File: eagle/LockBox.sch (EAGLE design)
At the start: 7 parts

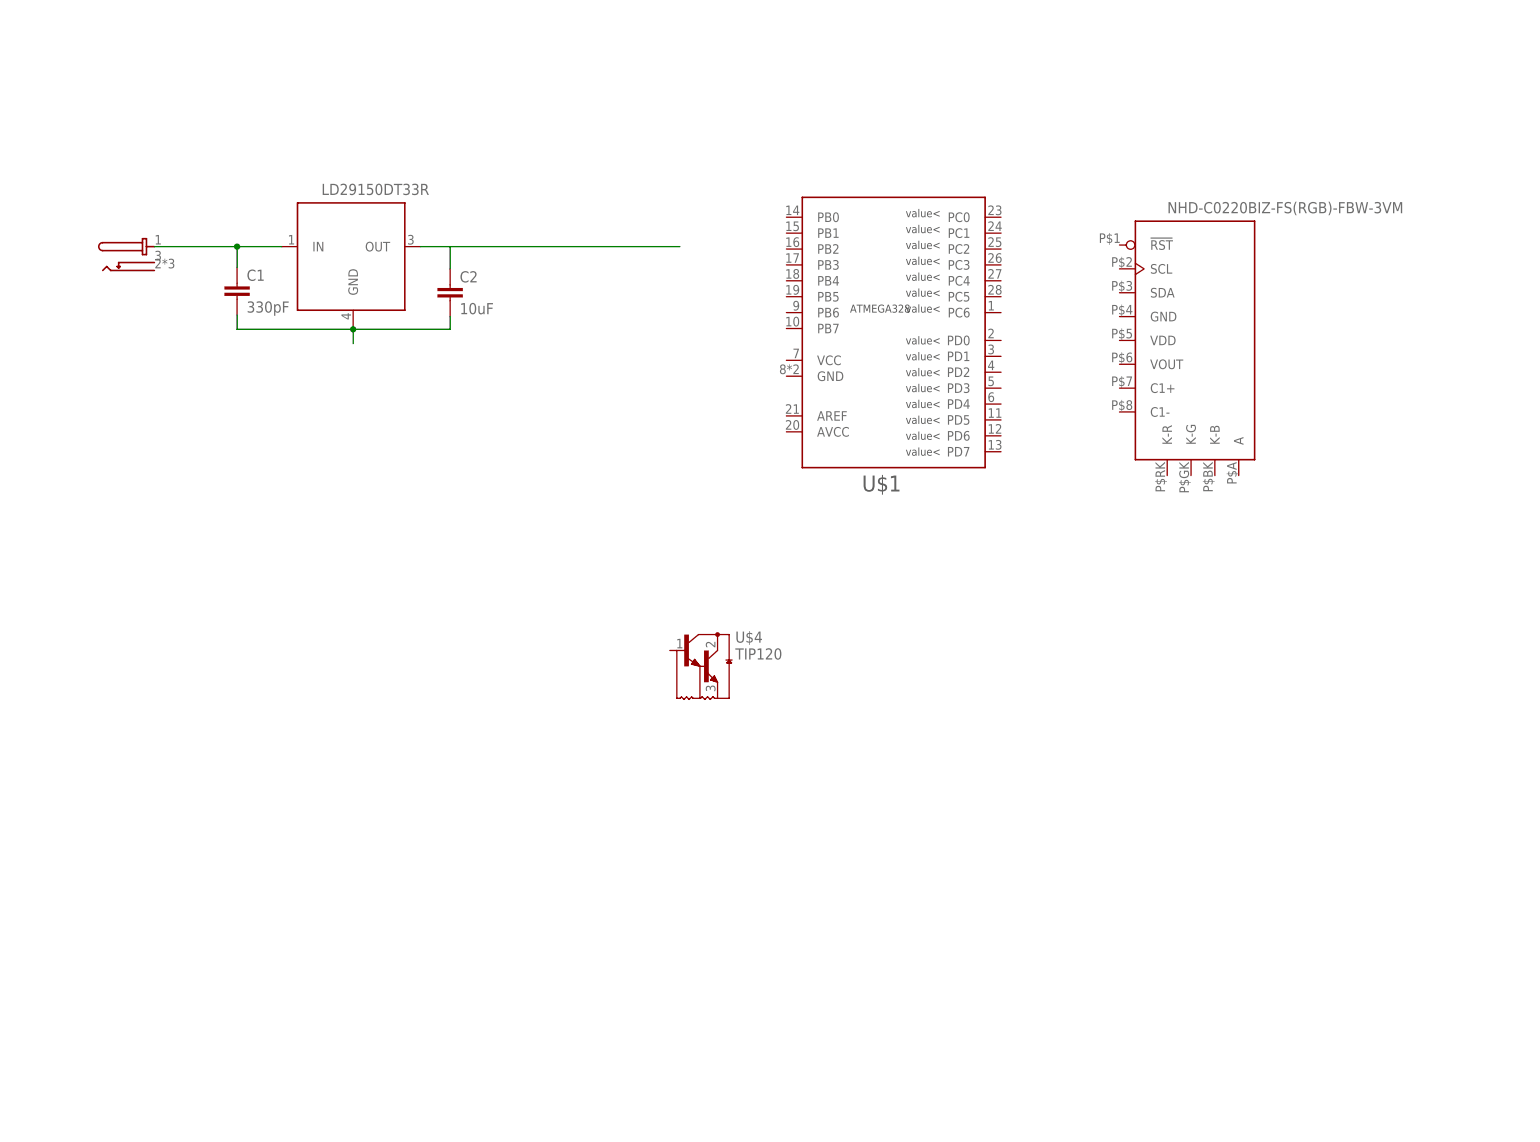
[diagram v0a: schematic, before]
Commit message: Finished the powersupply and LDO portion of the LockBox.sch, Added pwr/gnd and bypass cap to the ATMEL chip, updateded I2C pin attributes and added I2C bus.
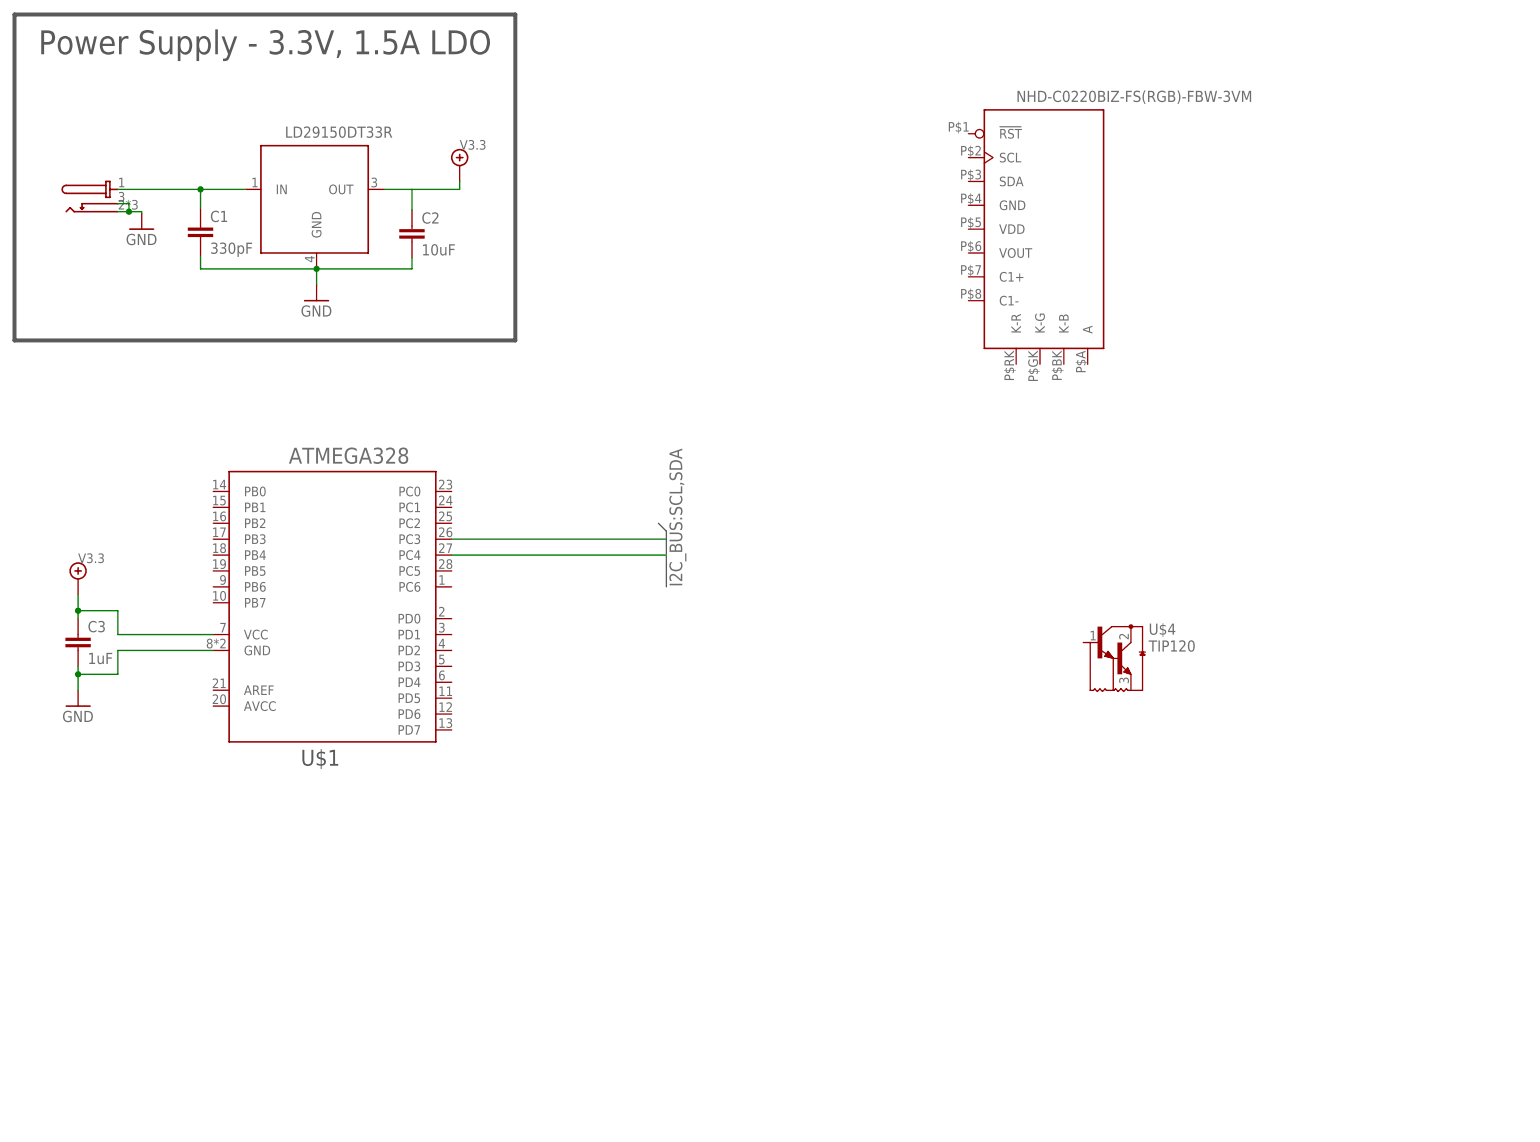
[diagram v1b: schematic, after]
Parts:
- added C3: 1uF, LockBox:C
- U$1: PC3 (none) -> SCL; PC4 (none) -> SDA
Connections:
- removed net N$2: C2.1, U$2.OUT
- removed net N$3: C1.2, C2.2, U$2.GND
- new net GND: C1.2, C2.2, C3.2, U$1.GND, U$2.GND, U$3.GND@1, U$3.GND@2
- new net P$1: C2.1, C3.1, U$1.VCC, U$2.OUT
- new net SCL: U$1.PC3
- new net SDA: U$1.PC4
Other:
- note added: "Power Supply - 3.3V, 1.5A LDO"
- moved on the sheet: C1, C2, U$4
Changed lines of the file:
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@@
 <setting verticaltext="up"/>
 </settings>
-<grid distance="0.005" unitdist="inch" unit="inch" style="lines" multiple="1" display="yes" altdistance="0.01" altunitdist="inch" altunit="inch"/>
+<grid distance="0.05" unitdist="inch" unit="inch" style="lines" multiple="1" display="yes" altdistance="0.01" altunitdist="inch" altunit="inch"/>
 <layers>
 <layer number="1" name="Top" color="4" fill="1" visible="no" active="no"/>
@@
 <parts>
 <part name="FRAME1" library="LockBox" deviceset="FRAME-LETTER" device=""/>
-<part name="U$1" library="LockBox" deviceset="ATMEGA328" device=""/>
 <part name="U$2" library="LockBox" deviceset="LD29150" device="" technology="DT33R"/>
 <part name="U$3" library="LockBox" deviceset="PJ_075" device="" technology="DH"/>
@@
 <part name="C1" library="LockBox" deviceset="C" device="" value="330pF"/>
 <part name="C2" library="LockBox" deviceset="C" device="" value="10uF"/>
+<part name="GND1" library="LockBox" deviceset="GND" device=""/>
+<part name="GND2" library="LockBox" deviceset="GND" device=""/>
+<part name="V1" library="LockBox" deviceset="V3.3" device=""/>
+<part name="U$1" library="LockBox" deviceset="ATMEGA328" device="">
+<attribute name="PC3" value="SCL"/>
+<attribute name="PC4" value="SDA"/>
+</part>
+<part name="C3" library="LockBox" deviceset="C" device="" value="1uF"/>
+<part name="GND3" library="LockBox" deviceset="GND" device=""/>
+<part name="V2" library="LockBox" deviceset="V3.3" device=""/>
 </parts>
 <sheets>
 <sheet>
 <plain>
+<wire x1="91.44" y1="180.34" x2="91.44" y2="128.27" width="0.635" layer="97"/>
+<wire x1="91.44" y1="128.27" x2="11.43" y2="128.27" width="0.635" layer="97"/>
+<wire x1="11.43" y1="128.27" x2="11.43" y2="180.34" width="0.635" layer="97"/>
+<wire x1="11.43" y1="180.34" x2="91.44" y2="180.34" width="0.635" layer="97"/>
+<text x="15.24" y="173.99" size="3.81" layer="97">Power Supply - 3.3V, 1.5A LDO</text>
 </plain>
 <instances>
 <instance part="FRAME1" gate="G$1" x="0" y="0"/>
 <instance part="FRAME1" gate="G$2" x="147.32" y="0"/>
-<instance part="U$1" gate="G$1" x="151.892" y="132.08"/>
-<instance part="U$2" gate="G$1" x="61.722" y="141.986"/>
-<instance part="U$3" gate="G$1" x="31.877" y="142.621"/>
-<instance part="U$4" gate="G$1" x="121.92" y="76.2"/>
-<instance part="U$5" gate="G$1" x="200.66" y="129.54"/>
-<instance part="C1" gate="G$1" x="46.99" y="137.414"/>
-<instance part="C2" gate="G$1" x="81.026" y="137.16"/>
+<instance part="U$2" gate="G$1" x="55.88" y="151.13"/>
+<instance part="U$3" gate="G$1" x="26.035" y="151.765"/>
+<instance part="U$4" gate="G$1" x="187.96" y="77.47"/>
+<instance part="U$5" gate="G$1" x="176.53" y="147.32"/>
+<instance part="C1" gate="G$1" x="41.148" y="146.812"/>
+<instance part="C2" gate="G$1" x="74.93" y="146.558"/>
+<instance part="GND1" gate="1" x="59.69" y="134.62"/>
+<instance part="GND2" gate="1" x="31.75" y="146.05"/>
+<instance part="V1" gate="G1" x="82.55" y="156.21"/>
+<instance part="U$1" gate="G$1" x="62.23" y="88.265">
+<attribute name="PC3" x="62.23" y="88.265" size="1.778" layer="96" display="off"/>
+<attribute name="PC4" x="62.23" y="88.265" size="1.778" layer="96" display="off"/>
+</instance>
+<instance part="C3" gate="G$1" x="21.59" y="81.28"/>
+<instance part="GND3" gate="1" x="21.59" y="69.85"/>
+<instance part="V2" gate="G1" x="21.59" y="90.17"/>
 </instances>
 <busses>
+<bus name="I2C_BUS:SCL,SDA">
+<segment>
+<wire x1="114.3" y1="99.06" x2="115.57" y2="97.79" width="0.762" layer="92"/>
+<wire x1="115.57" y1="97.79" x2="115.57" y2="88.9" width="0.762" layer="92"/>
+<label x="118.11" y="88.9" size="2.032" layer="95" rot="R90"/>
+</segment>
+</bus>
 </busses>
 <nets>
@@
 <segment>
 <pinref part="C1" gate="G$1" pin="1"/>
-<wire x1="46.99" y1="139.954" x2="46.99" y2="143.256" width="0.1524" layer="91"/>
+<wire x1="41.148" y1="149.352" x2="41.148" y2="152.4" width="0.1524" layer="91"/>
 <pinref part="U$2" gate="G$1" pin="IN"/>
-<wire x1="46.99" y1="143.256" x2="54.102" y2="143.256" width="0.1524" layer="91"/>
-<wire x1="46.99" y1="143.256" x2="33.782" y2="143.256" width="0.1524" layer="91"/>
-<junction x="46.99" y="143.256"/>
+<wire x1="41.148" y1="152.4" x2="48.26" y2="152.4" width="0.1524" layer="91"/>
+<wire x1="41.148" y1="152.4" x2="27.94" y2="152.4" width="0.1524" layer="91"/>
+<junction x="41.148" y="152.4"/>
 <pinref part="U$3" gate="G$1" pin="PWR"/>
 </segment>
 </net>
-<net name="N$2" class="0">
+<net name="GND" class="0">
+<segment>
+<pinref part="C2" gate="G$1" pin="2"/>
+<wire x1="74.93" y1="141.478" x2="74.93" y2="139.7" width="0.1524" layer="91"/>
+<pinref part="U$2" gate="G$1" pin="GND"/>
+<wire x1="74.93" y1="139.7" x2="59.69" y2="139.7" width="0.1524" layer="91"/>
+<pinref part="C1" gate="G$1" pin="2"/>
+<wire x1="59.69" y1="139.7" x2="41.148" y2="139.7" width="0.1524" layer="91"/>
+<wire x1="41.148" y1="139.7" x2="41.148" y2="141.732" width="0.1524" layer="91"/>
+<junction x="59.69" y="139.7"/>
+<wire x1="59.69" y1="139.7" x2="59.69" y2="137.16" width="0.1524" layer="91"/>
+<pinref part="GND1" gate="1" pin="GND"/>
+</segment>
+<segment>
+<pinref part="U$3" gate="G$1" pin="GND@1"/>
+<wire x1="27.94" y1="150.114" x2="29.718" y2="150.114" width="0.1524" layer="91"/>
+<wire x1="29.718" y1="150.114" x2="29.718" y2="148.844" width="0.1524" layer="91"/>
+<pinref part="U$3" gate="G$1" pin="GND@2"/>
+<wire x1="29.718" y1="148.844" x2="27.94" y2="148.844" width="0.1524" layer="91"/>
+<wire x1="29.718" y1="148.844" x2="31.75" y2="148.844" width="0.1524" layer="91"/>
+<wire x1="31.75" y1="148.844" x2="31.75" y2="148.59" width="0.1524" layer="91"/>
+<pinref part="GND2" gate="1" pin="GND"/>
+<junction x="29.718" y="148.844"/>
+</segment>
+<segment>
+<pinref part="U$1" gate="G$1" pin="GND"/>
+<wire x1="43.18" y1="78.74" x2="27.94" y2="78.74" width="0.1524" layer="91"/>
+<wire x1="27.94" y1="78.74" x2="27.94" y2="74.93" width="0.1524" layer="91"/>
+<wire x1="27.94" y1="74.93" x2="21.59" y2="74.93" width="0.1524" layer="91"/>
+<pinref part="C3" gate="G$1" pin="2"/>
+<wire x1="21.59" y1="74.93" x2="21.59" y2="76.2" width="0.1524" layer="91"/>
+<pinref part="GND3" gate="1" pin="GND"/>
+<wire x1="21.59" y1="74.93" x2="21.59" y2="72.39" width="0.1524" layer="91"/>
+<junction x="21.59" y="74.93"/>
+</segment>
+</net>
+<net name="P$1" class="0">
 <segment>
 <pinref part="C2" gate="G$1" pin="1"/>
-<wire x1="81.026" y1="139.7" x2="81.026" y2="143.256" width="0.1524" layer="91"/>
+<wire x1="74.93" y1="149.098" x2="74.93" y2="152.4" width="0.1524" layer="91"/>
 <pinref part="U$2" gate="G$1" pin="OUT"/>
-<wire x1="76.327" y1="143.256" x2="81.026" y2="143.256" width="0.1524" layer="91"/>
-<wire x1="81.026" y1="143.256" x2="117.729" y2="143.256" width="0.1524" layer="91"/>
-</segment>
-</net>
-<net name="N$3" class="0">
-<segment>
-<pinref part="C2" gate="G$1" pin="2"/>
-<wire x1="81.026" y1="132.08" x2="81.026" y2="130.048" width="0.1524" layer="91"/>
-<pinref part="U$2" gate="G$1" pin="GND"/>
-<wire x1="81.026" y1="130.048" x2="65.532" y2="130.048" width="0.1524" layer="91"/>
-<wire x1="65.532" y1="130.048" x2="65.532" y2="130.556" width="0.1524" layer="91"/>
-<pinref part="C1" gate="G$1" pin="2"/>
-<wire x1="65.532" y1="130.048" x2="46.99" y2="130.048" width="0.1524" layer="91"/>
-<wire x1="46.99" y1="130.048" x2="46.99" y2="132.334" width="0.1524" layer="91"/>
-<junction x="65.532" y="130.048"/>
-<wire x1="65.532" y1="130.048" x2="65.532" y2="127.762" width="0.1524" layer="91"/>
-</segment>
-</net>
+<wire x1="70.485" y1="152.4" x2="74.93" y2="152.4" width="0.1524" layer="91"/>
+<wire x1="74.93" y1="152.4" x2="82.55" y2="152.4" width="0.1524" layer="91"/>
+<pinref part="V1" gate="G1" pin="P$1"/>
+<wire x1="82.55" y1="152.4" x2="82.55" y2="153.67" width="0.1524" layer="91"/>
+</segment>
+<segment>
+<pinref part="U$1" gate="G$1" pin="VCC"/>
+<wire x1="43.18" y1="81.28" x2="27.94" y2="81.28" width="0.1524" layer="91"/>
+<wire x1="27.94" y1="81.28" x2="27.94" y2="85.09" width="0.1524" layer="91"/>
+<wire x1="27.94" y1="85.09" x2="21.59" y2="85.09" width="0.1524" layer="91"/>
+<pinref part="C3" gate="G$1" pin="1"/>
+<wire x1="21.59" y1="85.09" x2="21.59" y2="83.82" width="0.1524" layer="91"/>
+<pinref part="V2" gate="G1" pin="P$1"/>
+<wire x1="21.59" y1="85.09" x2="21.59" y2="87.63" width="0.1524" layer="91"/>
+<junction x="21.59" y="85.09"/>
+</segment>
+</net>
+<net name="SCL" class="0">
+<segment>
+<pinref part="U$1" gate="G$1" pin="PC3"/>
+<wire x1="115.57" y1="96.52" x2="81.28" y2="96.52" width="0.1524" layer="91"/>
+</segment>
+</net>
+<net name="SDA" class="0">
+<segment>
+<pinref part="U$1" gate="G$1" pin="PC4"/>
+<wire x1="115.57" y1="93.98" x2="81.28" y2="93.98" width="0.1524" layer="91"/>
+</segment>
+</net>
